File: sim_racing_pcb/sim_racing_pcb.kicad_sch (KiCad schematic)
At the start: 25 parts, among them J1 Pedales, J10 Encoder - IZQ, J11 Display TFT, J12 GND, J13 GND, J14 3V3, J15 5V, J2 Paddle_Shift_R, J3 Paddle_Shift_L, J4 BTN 1, J5 Leds, J6 AS5600, J7 BTN 2, J8 Encoder - DER, J9 Encoder - MID, U6 Pico

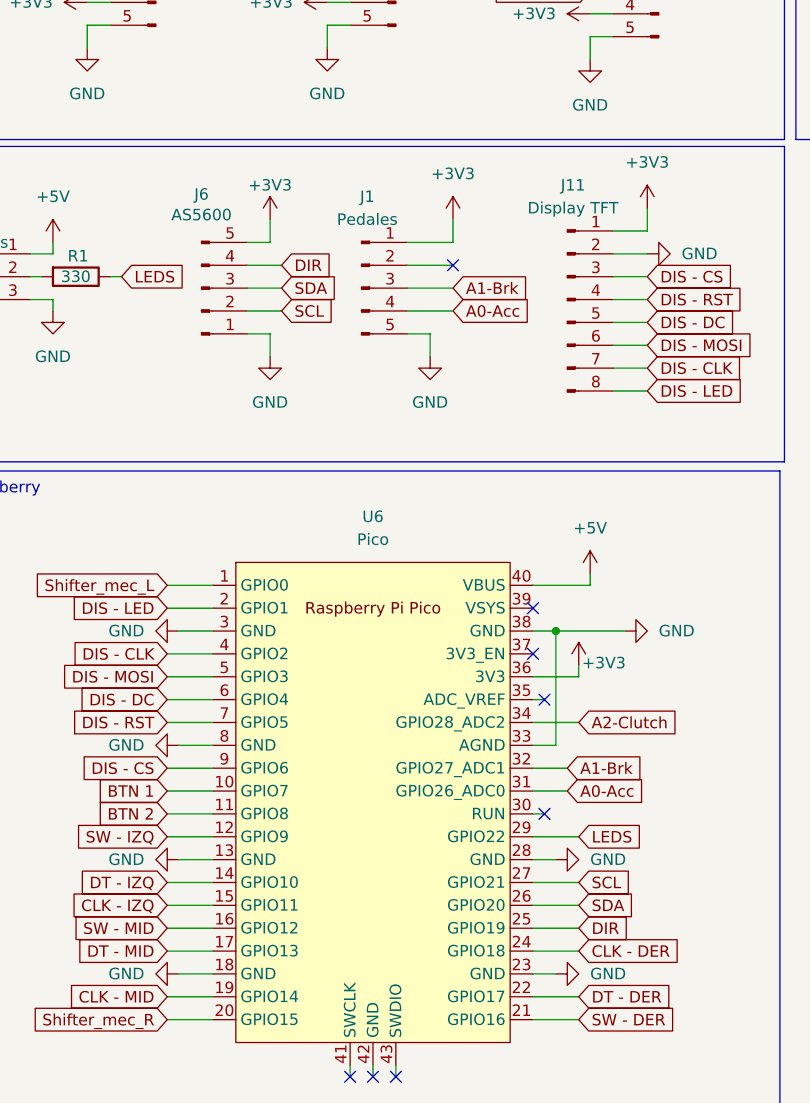
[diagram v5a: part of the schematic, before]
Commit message: Modify usb and as5600 connectors for unique 6 cable molex
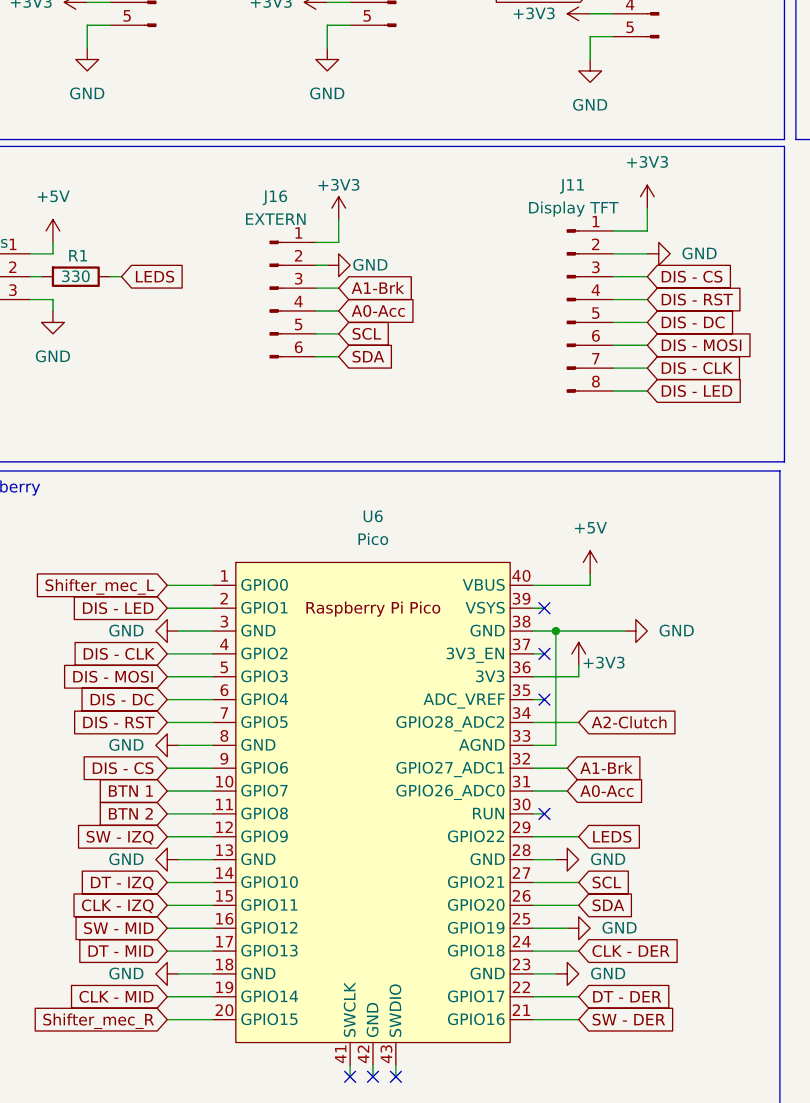
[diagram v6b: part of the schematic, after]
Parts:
- removed J1: Pedales, Connector_Molex:Molex_KK-254_AE-6410-05A_1x05_P2.54mm_Vertical, symbol Connector:Conn_01x05_Pin
- removed J6: AS5600, Connector_Molex:Molex_KK-254_AE-6410-05A_1x05_P2.54mm_Vertical, symbol Connector:Conn_01x05_Pin
- added J16: EXTERN, Connector_Molex:Molex_KK-254_AE-6410-06A_1x06_P2.54mm_Vertical, symbol Connector:Conn_01x06_Pin
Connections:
- net DIR is gone; now on net GND: U6.25 (GPIO19)
- net +3V3: now also J16.1 (Pin_1)
- net A0-Acc: now also J16.4 (Pin_4)
- net A1-Brk: now also J16.3 (Pin_3)
- net GND: now also J16.2 (Pin_2)
- net SCL: now also J16.5 (Pin_5)
- net SDA: now also J16.6 (Pin_6)
- no-connect marks 8 -> 7
